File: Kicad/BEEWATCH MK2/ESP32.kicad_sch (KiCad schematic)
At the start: 40 parts, among them J1 USB_C_Receptacle_USB2.0_16P, Q1 DMG6968U, SW1 TK-074-4, SW2 TK-074-4, U1 ESP32-S3FH4R2, Y1 40MHz, Y2 32.768KHz

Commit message: Antenna layout completed
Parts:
- added TP2: TestPoint, TestPoint:TestPoint_Pad_D1.0mm, symbol Connector:TestPoint
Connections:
- net GND: now also TP2.1
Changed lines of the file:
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@@
 	(wire
 		(pts
+			(xy 337.82 134.62) (xy 337.82 138.43)
+		)
+		(stroke
+			(width 0)
+			(type default)
+		)
+	)
+	(wire
+		(pts
 			(xy 212.09 110.49) (xy 250.19 110.49)
 		)
@@
 	(symbol
 		(lib_id "power:GND")
+		(at 337.82 138.43 0)
+		(unit 1)
+		(exclude_from_sim no)
+		(in_bom yes)
+		(on_board yes)
+		(dnp no)
+		(property "Reference" "#PWR066"
+			(at 337.82 144.78 0)
+			(effects
+				(font
+					(size 1.27 1.27)
+				)
+				(hide yes)
+			)
+		)
+		(property "Value" "GND"
+			(at 343.408 139.954 0)
+			(effects
+				(font
+					(size 1.27 1.27)
+				)
+				(justify right)
+			)
+		)
+		(property "Footprint" ""
+			(at 337.82 138.43 0)
+			(effects
+				(font
+					(size 1.27 1.27)
+				)
+				(hide yes)
+			)
+		)
+		(property "Datasheet" ""
+			(at 337.82 138.43 0)
+			(effects
+				(font
+					(size 1.27 1.27)
+				)
+				(hide yes)
+			)
+		)
+		(property "Description" "Power symbol creates a global label with name \"GND\" , ground"
+			(at 337.82 138.43 0)
+			(effects
+				(font
+					(size 1.27 1.27)
+				)
+				(hide yes)
+			)
+		)
+		(pin "1"
+		)
+		(instances
+			(project "BEEWATCH MK2"
+				(path "/e9c5fb53-480b-4989-8495-a3341ee99514/56d77f8e-c069-456f-a514-fdde13f048cd"
+					(reference "#PWR066")
+					(unit 1)
+				)
+			)
+		)
+	)
+	(symbol
+		(lib_id "power:GND")
 		(at 73.66 160.02 0)
 		(unit 1)
@@
 	)
 	(symbol
+		(lib_id "Connector:TestPoint")
+		(at 337.82 134.62 0)
+		(mirror y)
+		(unit 1)
+		(exclude_from_sim no)
+		(in_bom yes)
+		(on_board yes)
+		(dnp no)
+		(property "Reference" "TP2"
+			(at 339.344 131.572 0)
+			(effects
+				(font
+					(size 1.27 1.27)
+				)
+				(justify right)
+			)
+		)
+		(property "Value" "TestPoint"
+			(at 339.344 134.112 0)
+			(effects
+				(font
+					(size 1.27 1.27)
+				)
+				(justify right)
+				(hide yes)
+			)
+		)
+		(property "Footprint" "TestPoint:TestPoint_Pad_D1.0mm"
+			(at 332.74 134.62 0)
+			(effects
+				(font
+					(size 1.27 1.27)
+				)
+				(hide yes)
+			)
+		)
+		(property "Datasheet" "~"
+			(at 332.74 134.62 0)
+			(effects
+				(font
+					(size 1.27 1.27)
+				)
+				(hide yes)
+			)
+		)
+		(property "Description" "test point"
+			(at 337.82 134.62 0)
+			(effects
+				(font
+					(size 1.27 1.27)
+				)
+				(hide yes)
+			)
+		)
+		(pin "1"
+		)
+		(instances
+			(project "BEEWATCH MK2"
+				(path "/e9c5fb53-480b-4989-8495-a3341ee99514/56d77f8e-c069-456f-a514-fdde13f048cd"
+					(reference "TP2")
+					(unit 1)
+				)
+			)
+		)
+	)
+	(symbol
 		(lib_id "Device:R_Small")
 		(at 231.14 140.97 90)
@@
 		(fields_autoplaced yes)
 		(property "Reference" "TP1"
-			(at 321.31 147.3199 90)
+			(at 321.31 148.5899 90)
 			(effects
 				(font
@@
 				)
 				(justify left)
+				(hide yes)
 			)
 		)

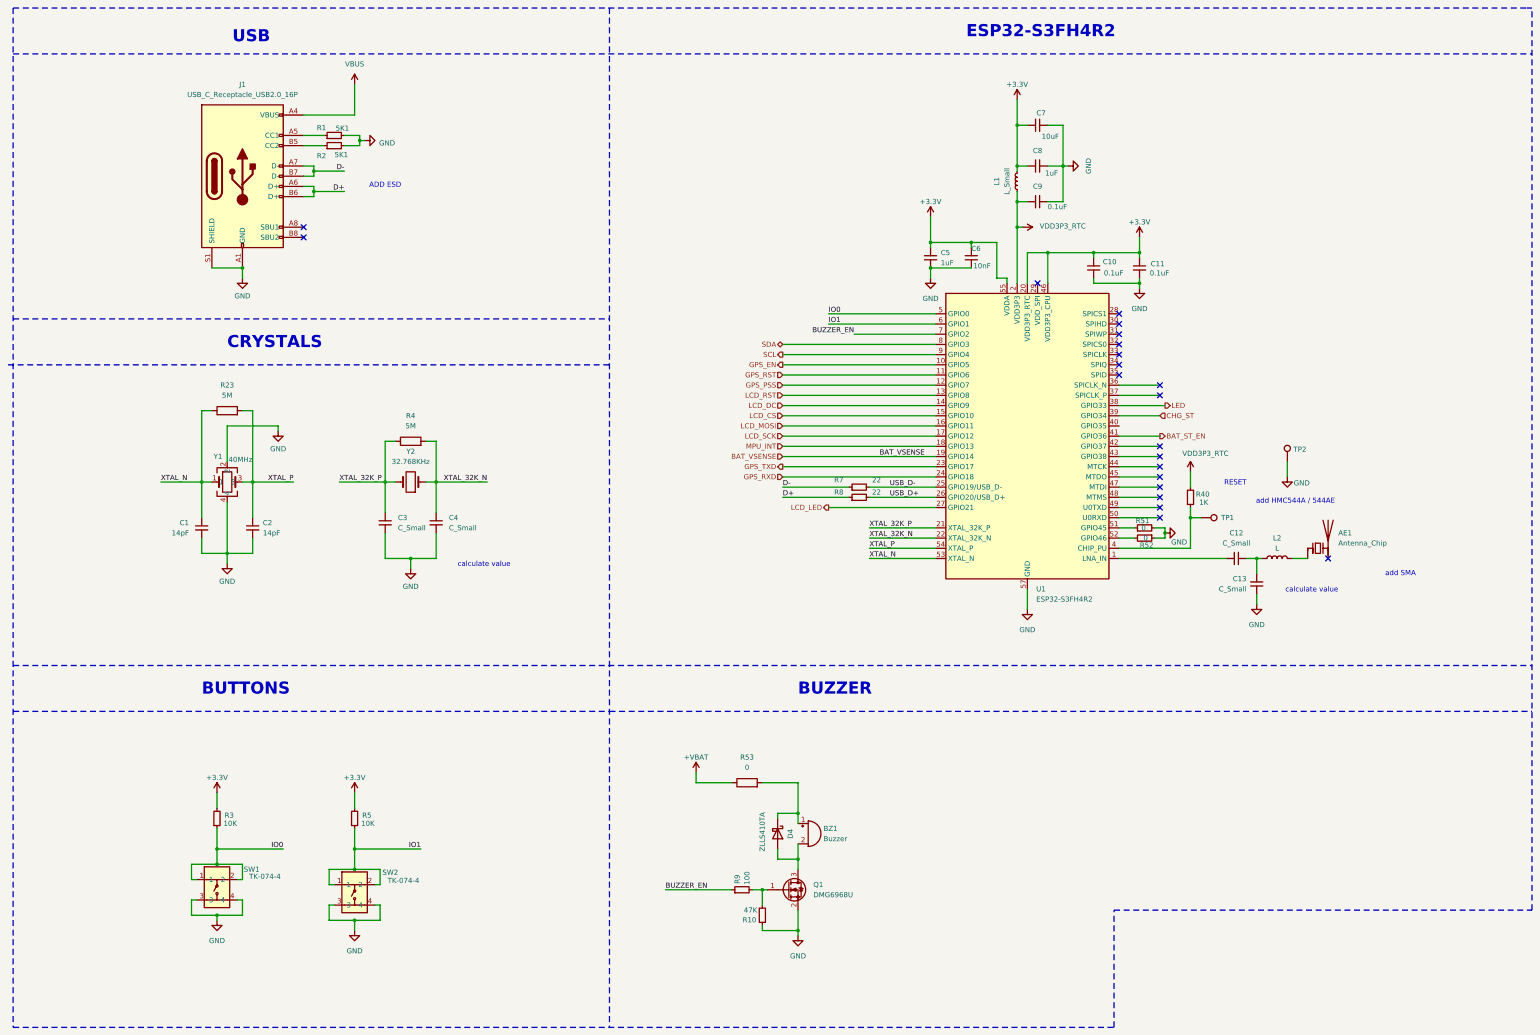
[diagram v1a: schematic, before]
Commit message: Antenna and Schematic correction
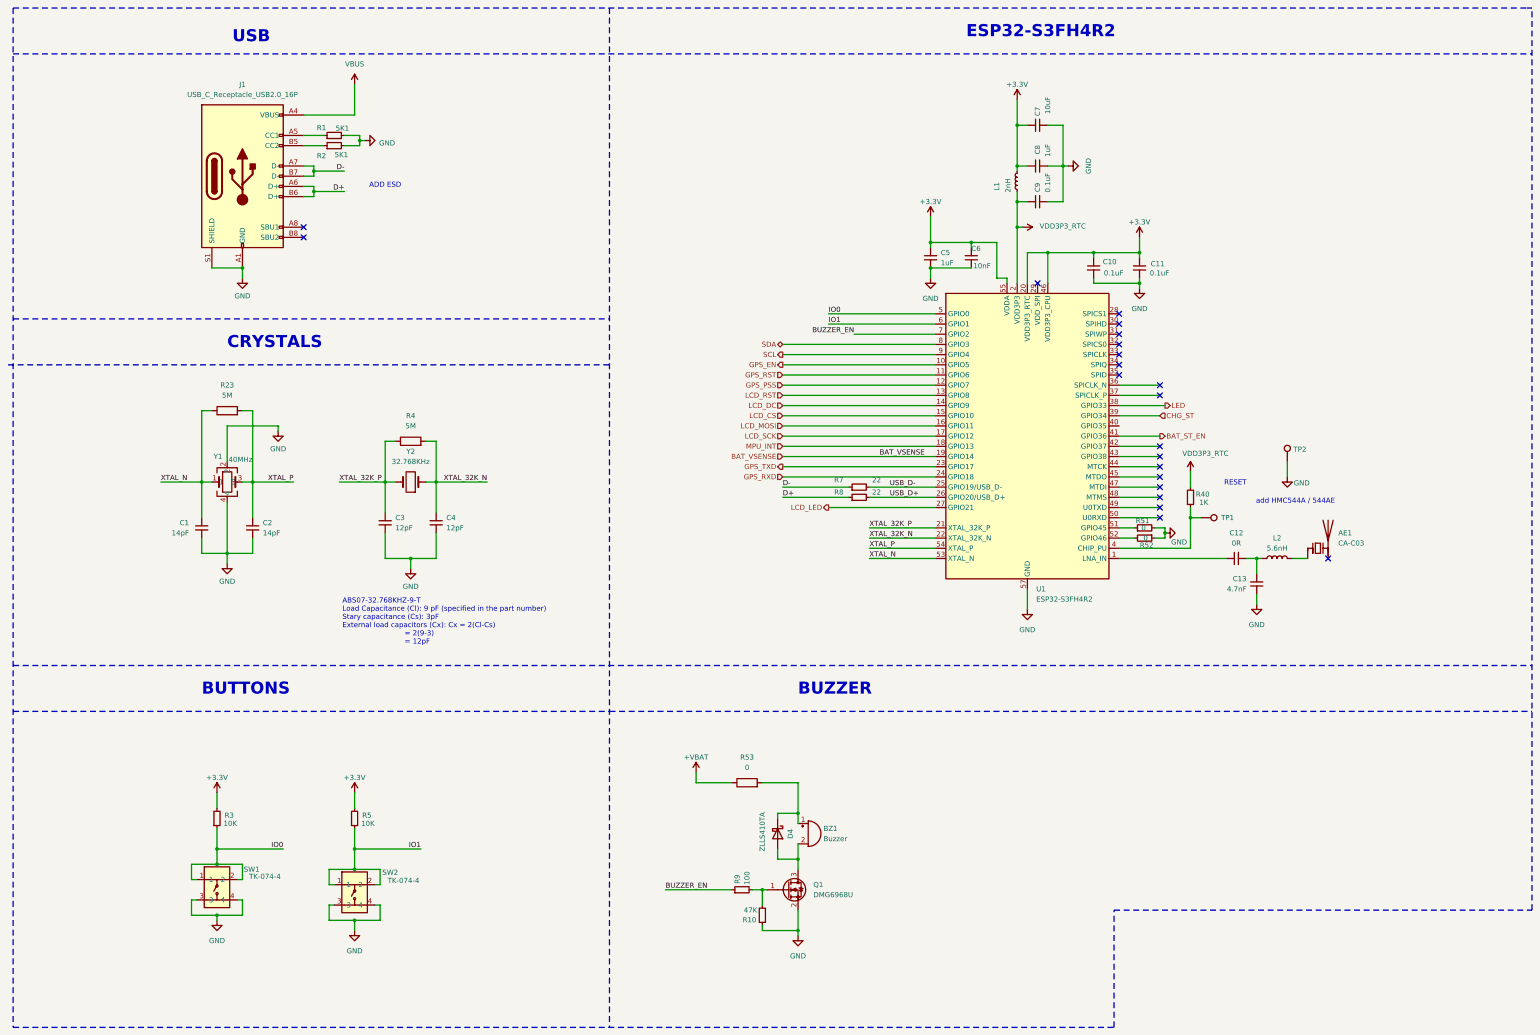
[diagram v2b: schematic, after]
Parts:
- AE1: value Antenna_Chip -> CA-C03
- C12: value C_Small -> 0R
- C13: value C_Small -> 4.7nF
- C3, C4: value C_Small -> 12pF
- L1: value L_Small -> 2nH
- L2: value L -> 5.6nH
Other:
- note added: "ABS07-32.768KHZ-9-T Load Capacitance (Cl): 9 pF (specified in the part number) Stary capacitance (Cs): 3pF External load capacitors (Cx): Cx = 2(Cl-Cs) = 2(9-3) = 12pF"
- note removed: "add SMA"
- note removed: "calculate value"
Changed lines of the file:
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@@
 	(generator_version "9.0")
 	(paper "A3")
-	(text "add SMA\n"
-		(exclude_from_sim no)
-		(at 366.014 162.56 0)
-		(effects
-			(font
-				(size 1.27 1.27)
-			)
-		)
-	)
 	(text "BUZZER\n"
 		(exclude_from_sim no)
@@
 		)
 	)
-	(text "calculate value"
-		(exclude_from_sim no)
-		(at 343.916 166.624 0)
-		(effects
-			(font
-				(size 1.27 1.27)
-			)
-		)
-	)
 	(text "add HMC544A / 544AE"
 		(exclude_from_sim no)
@@
 		)
 	)
-	(text "calculate value"
+	(text "ABS07-32.768KHZ-9-T\nLoad Capacitance (Cl): 9 pF (specified in the part number)\nStary capacitance (Cs): 3pF\nExternal load capacitors (Cx): Cx = 2(Cl-Cs)\n							= 2(9-3)\n							= 12pF"
 		(exclude_from_sim no)
-		(at 137.668 160.274 0)
+		(at 102.362 174.498 0)
 		(effects
 			(font
 				(size 1.27 1.27)
 			)
+			(justify left)
 		)
 	)
@@
 			(width 0)
 			(type default)
+			(color 255 234 16 1)
 		)
 	)
@@
 		)
 	)
+	(netclass_flag ""
+		(length 2.54)
+		(shape round)
+		(at 306.07 158.75 180)
+		(fields_autoplaced yes)
+		(effects
+			(font
+				(size 1.27 1.27)
+			)
+			(justify right bottom)
+		)
+		(property "Netclass" "ANT FEED LINE"
+			(at 306.7685 161.29 0)
+			(effects
+				(font
+					(size 1.27 1.27)
+				)
+				(justify left)
+			)
+		)
+		(property "Component Class" "ANT"
+			(at 306.7685 159.8295 0)
+			(effects
+				(font
+					(size 1.27 1.27)
+					(italic yes)
+				)
+				(justify left)
+				(hide yes)
+			)
+		)
+	)
 	(symbol
 		(lib_id "SM_CRYSTAL:2x3")
@@
 			)
 		)
-		(property "Value" "Antenna_Chip"
+		(property "Value" "CA-C03"
 			(at 350.52 154.9399 0)
 			(effects
@@
 			)
 		)
-		(property "Value" "C_Small"
+		(property "Value" "4.7nF"
 			(at 327.66 166.3635 0)
 			(effects
@@
 		(on_board yes)
 		(dnp no)
-		(fields_autoplaced yes)
 		(property "Reference" "L1"
-			(at 265.43 64.77 90)
+			(at 265.43 67.056 90)
 			(effects
 				(font
 					(size 1.27 1.27)
 				)
+				(justify right)
 			)
 		)
-		(property "Value" "L_Small"
-			(at 267.97 64.77 90)
+		(property "Value" "2nH"
+			(at 268.224 67.564 90)
 			(effects
 				(font
 					(size 1.27 1.27)
 				)
+				(justify right)
 			)
 		)
@@
 		(dnp no)
 		(property "Reference" "C8"
-			(at 275.5963 57.15 90)
+			(at 275.59 56.896 0)
 			(effects
 				(font
@@
 		)
 		(property "Value" "1uF"
-			(at 280.67 62.738 90)
+			(at 278.13 58.674 0)
 			(effects
 				(font
@@
 		(fields_autoplaced yes)
 		(property "Reference" "C4"
-			(at 128.905 148.5962 0)
+			(at 128.27 148.5962 0)
 			(effects
 				(font
@@
 			)
 		)
-		(property "Value" "C_Small"
-			(at 128.905 151.1362 0)
+		(property "Value" "12pF"
+			(at 128.27 151.1362 0)
 			(effects
 				(font
@@
 			)
 		)
-		(property "Value" "C_Small"
+		(property "Value" "0R"
 			(at 325.1263 154.94 90)
 			(effects
@@
 			)
 		)
-		(property "Value" "L"
+		(property "Value" "5.6nH"
 			(at 335.28 156.21 90)
 			(effects
@@
 		(dnp no)
 		(property "Reference" "C7"
-			(at 277.622 47.752 90)
+			(at 275.59 48.514 0)
 			(effects
 				(font
@@
 		)
 		(property "Value" "10uF"
-			(at 276.606 53.594 90)
+			(at 278.13 43.688 0)
 			(effects
 				(font
@@
 		(fields_autoplaced yes)
 		(property "Reference" "C3"
-			(at 116.205 148.5962 0)
+			(at 115.57 148.5962 0)
 			(effects
 				(font
@@
 			)
 		)
-		(property "Value" "C_Small"
-			(at 116.205 151.1362 0)
+		(property "Value" "12pF"
+			(at 115.57 151.1362 0)
 			(effects
 				(font
@@
 		(dnp no)
 		(property "Reference" "C9"
-			(at 275.5963 66.04 90)
+			(at 275.59 66.294 0)
 			(effects
 				(font
@@
 		)
 		(property "Value" "0.1uF"
-			(at 282.956 71.12 90)
+			(at 278.13 67.564 0)
 			(effects
 				(font

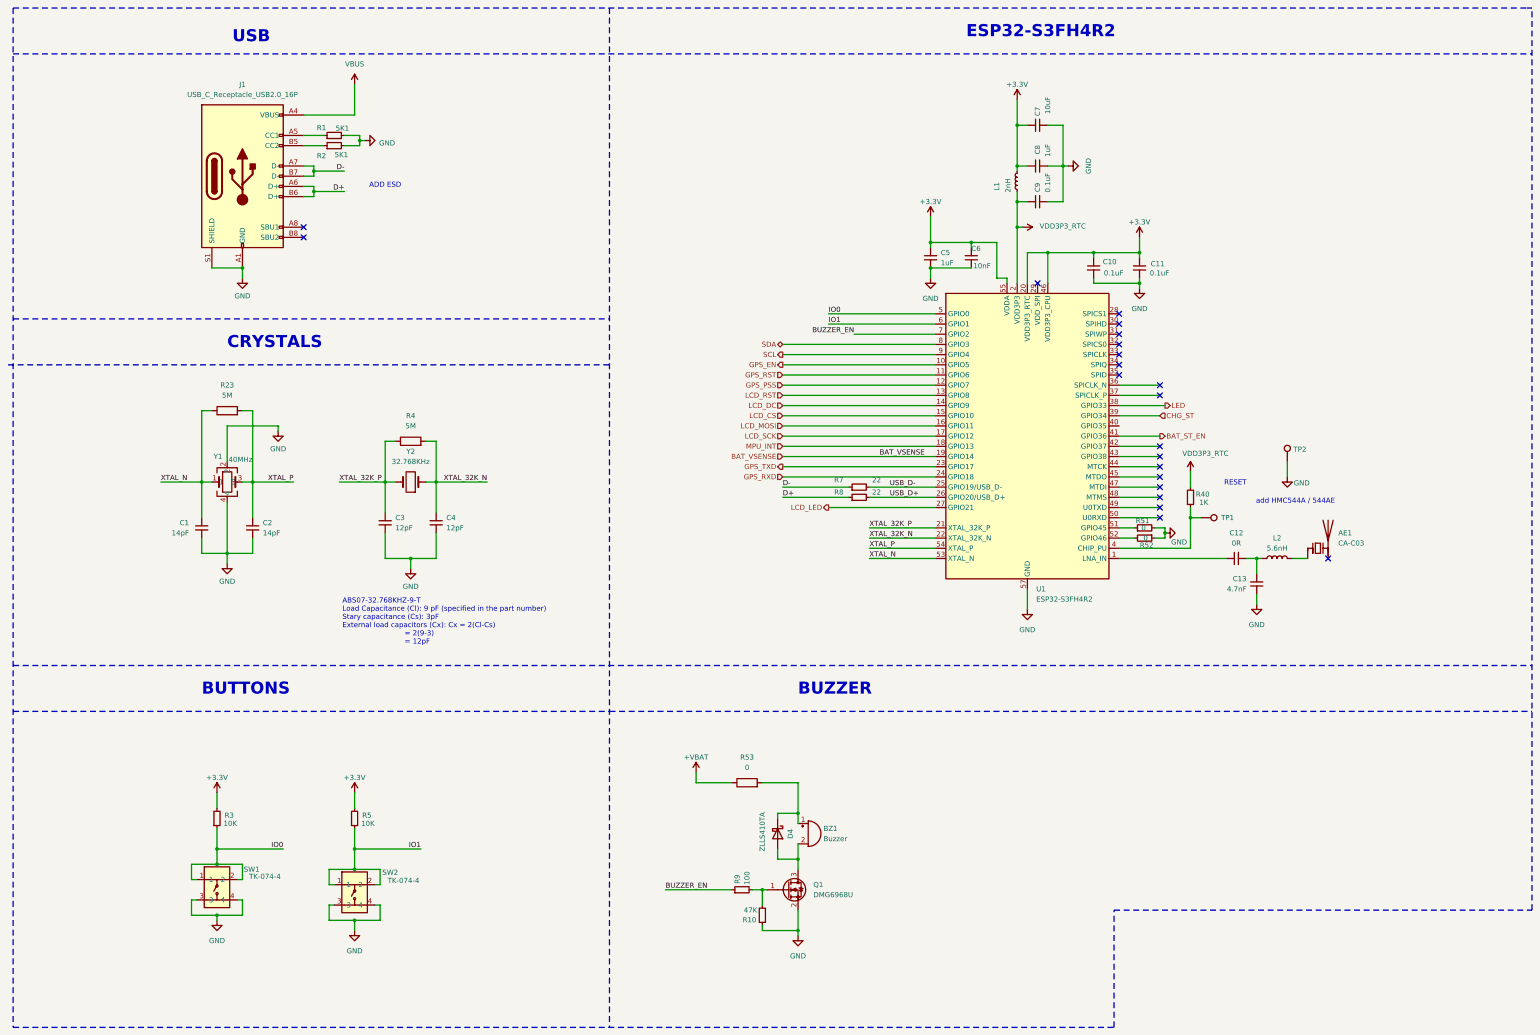
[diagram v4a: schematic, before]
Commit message: Updating MPN
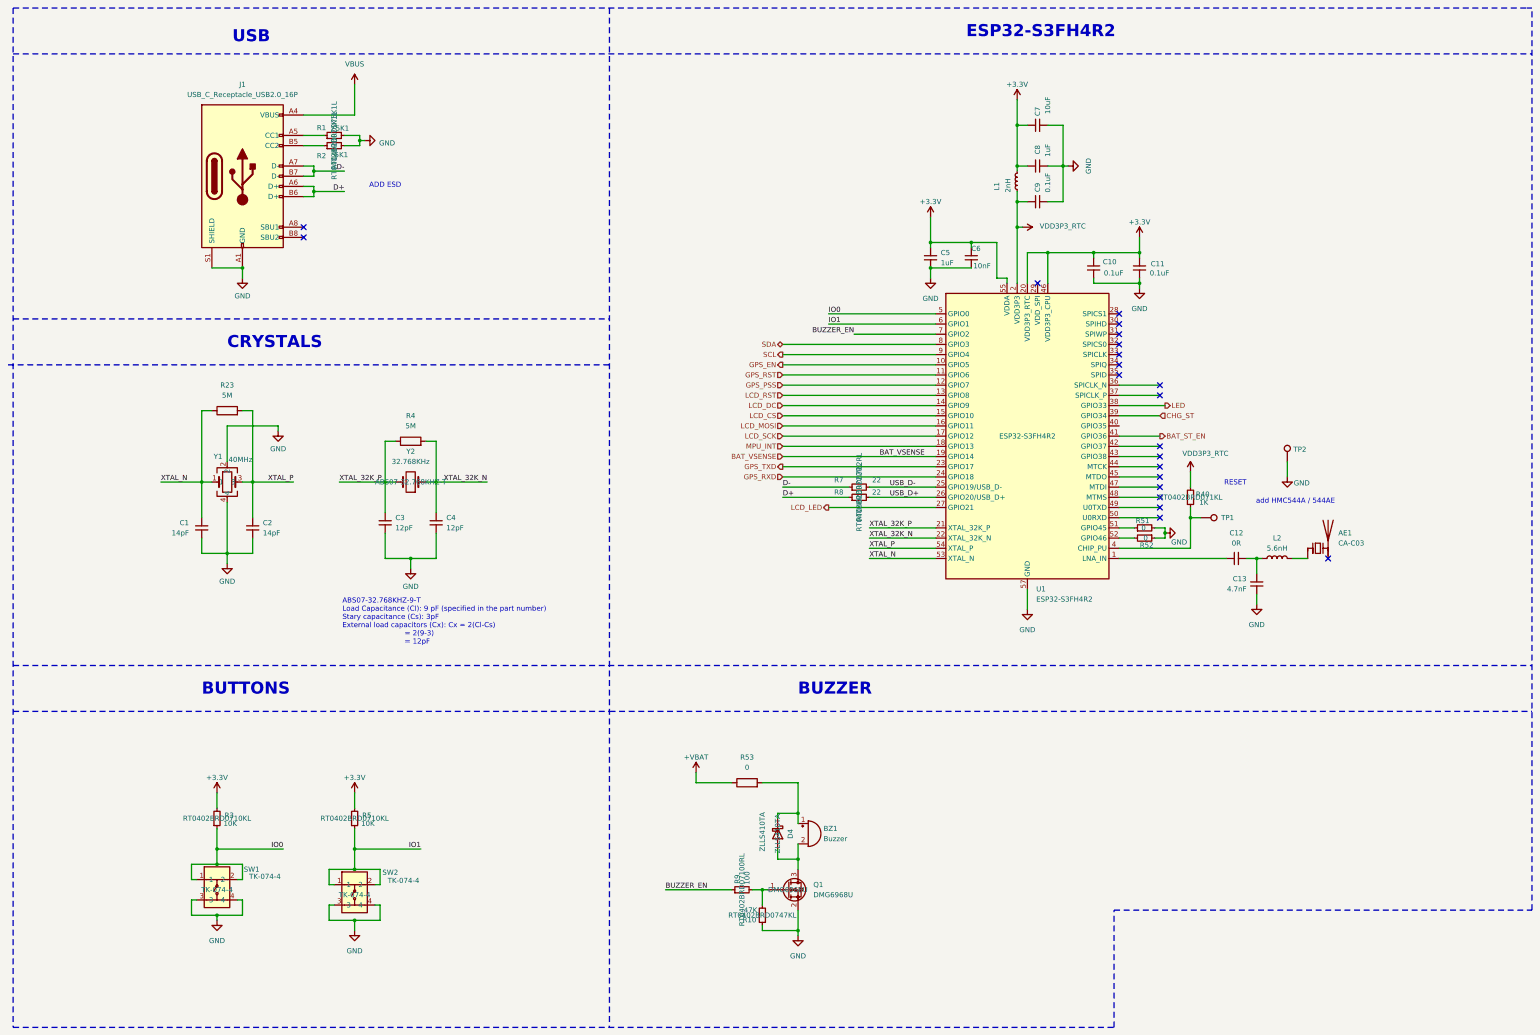
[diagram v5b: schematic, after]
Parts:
- D4: MPN (none) -> ZLLS410TA
- Q1: MPN (none) -> DMG6968U
- R1, R2: MPN (none) -> RT0402BRD075K1L
- R10: MPN (none) -> RT0402BRD0747KL
- R3, R5: MPN (none) -> RT0402BRD0710KL
- R40: MPN (none) -> RT0402BRD071KL
- R7, R8: MPN (none) -> RT0402BRD0722RL
- R9: MPN (none) -> RT0402BRD07100RL
- SW1, SW2: MPN (none) -> TK-074-4
- U1: MPN (none) -> ESP32-S3FH4R2
- Y2: MPN (none) -> ABS07-32.768KHZ-T
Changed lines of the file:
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@@
 			)
 		)
-		(property "MPN" ""
+		(property "MPN" "DMG6968U"
 			(at 213.36 241.3 0)
 			(effects
@@
 			)
 		)
-		(property "MPN" ""
+		(property "MPN" "TK-074-4"
 			(at 105.41 242.57 0)
 			(effects
@@
 			)
 		)
-		(property "MPN" ""
+		(property "MPN" "RT0402BRD0710KL "
 			(at 105.41 223.52 0)
 			(effects
@@
 			)
 		)
-		(property "MPN" ""
+		(property "MPN" "RT0402BRD075K1L "
 			(at 100.33 53.34 0)
 			(effects
@@
 			)
 		)
-		(property "MPN" ""
+		(property "MPN" "TK-074-4"
 			(at 71.12 241.3 0)
 			(effects
@@
 			)
 		)
-		(property "MPN" ""
+		(property "MPN" "ABS07-32.768KHZ-T"
 			(at 119.38 139.7 0)
 			(effects
@@
 			)
 		)
-		(property "MPN" ""
+		(property "MPN" "RT0402BRD0722RL "
 			(at 231.14 143.51 0)
 			(effects
@@
 			)
 		)
-		(property "MPN" ""
+		(property "MPN" "ESP32-S3FH4R2"
 			(at 273.05 128.27 0)
 			(effects
@@
 			)
 		)
-		(property "MPN" ""
+		(property "MPN" "RT0402BRD0722RL "
 			(at 231.14 140.97 0)
 			(effects
@@
 			)
 		)
-		(property "MPN" ""
+		(property "MPN" "RT0402BRD075K1L "
 			(at 100.33 55.88 0)
 			(effects
@@
 			)
 		)
-		(property "MPN" ""
+		(property "MPN" "RT0402BRD07100RL "
 			(at 201.93 241.3 0)
 			(effects
@@
 			)
 		)
-		(property "MPN" ""
+		(property "MPN" "RT0402BRD0710KL "
 			(at 71.12 223.52 0)
 			(effects
@@
 			)
 		)
-		(property "MPN" ""
+		(property "MPN" "RT0402BRD0747KL "
 			(at 207.01 247.65 0)
 			(effects
@@
 			)
 		)
-		(property "MPN" ""
+		(property "MPN" "ZLLS410TA"
 			(at 210.82 227.33 0)
 			(effects
@@
 			)
 		)
-		(property "MPN" ""
+		(property "MPN" "RT0402BRD071KL "
 			(at 313.69 143.51 0)
 			(effects
